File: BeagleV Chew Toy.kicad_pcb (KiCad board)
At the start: 2 copper layers, 69.2 x 59.8 mm, 151 parts, among them J1 Conn_02x05_Counter_Clockwise, J2 Conn_02x05_Counter_Clockwise, J3 Conn_02x05_Counter_Clockwise, U1 74HC245, U2 74HC245, U3 74HC245, U4 74HC245

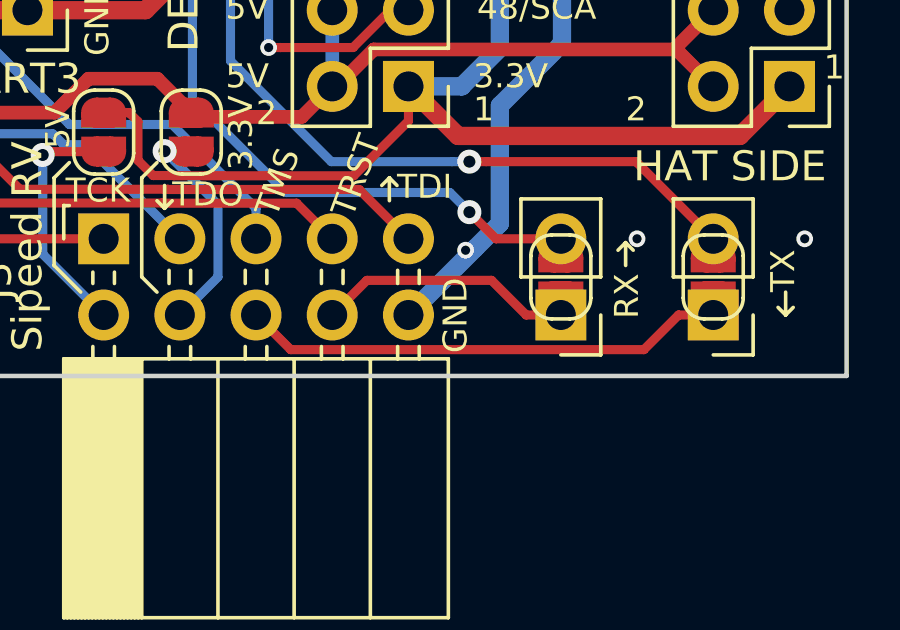
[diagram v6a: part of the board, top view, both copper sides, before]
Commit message: fixup: swap RX/TX on Sipeed connector
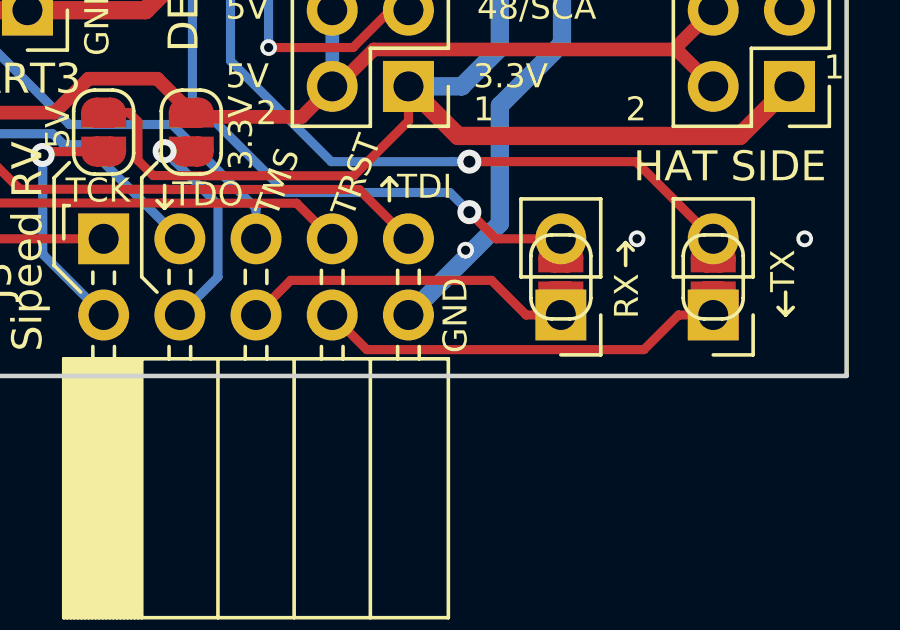
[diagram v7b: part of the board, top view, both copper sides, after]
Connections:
- JP36 pad 1: Net-(J3-Pad6) -> Net-(J3-Pad8)
- JP37 pad 1: Net-(J3-Pad6) -> Net-(J3-Pad8)
- JP38 pad 1: Net-(J3-Pad8) -> Net-(J3-Pad6)
- JP39 pad 1: Net-(J3-Pad8) -> Net-(J3-Pad6)
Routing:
- net Net-(J3-Pad8): track 8.58 -> 13.7 mm
- net Net-(J3-Pad6): track 16.2 -> 11.1 mm
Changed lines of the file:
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@@
       ))
     (pad 1 smd custom (at -0.65 0 90) (size 1 0.5) (layers Top F.Mask)
-      (net 56 "Net-(J3-Pad8)") (zone_connect 2)
+      (net 57 "Net-(J3-Pad6)") (zone_connect 2)
       (options (clearance outline) (anchor rect))
       (primitives
@@
       (net 20 /GPIO13/RX))
     (pad 1 thru_hole rect (at 0 0 180) (size 1.7 1.7) (drill 1) (layers *.Cu *.Mask)
-      (net 56 "Net-(J3-Pad8)"))
+      (net 57 "Net-(J3-Pad6)"))
     (model ${KISYS3DMOD}/Connector_PinHeader_2.54mm.3dshapes/PinHeader_1x02_P2.54mm_Vertical.wrl
       (at (xyz 0 0 0))
@@
       ))
     (pad 1 smd custom (at -0.65 0 90) (size 1 0.5) (layers Top F.Mask)
-      (net 57 "Net-(J3-Pad6)") (zone_connect 2)
+      (net 56 "Net-(J3-Pad8)") (zone_connect 2)
       (options (clearance outline) (anchor rect))
       (primitives
@@
       (net 21 /GPIO14/TX))
     (pad 1 thru_hole rect (at 0 0 180) (size 1.7 1.7) (drill 1) (layers *.Cu *.Mask)
-      (net 57 "Net-(J3-Pad6)"))
+      (net 56 "Net-(J3-Pad8)"))
     (model ${KISYS3DMOD}/Connector_PinHeader_2.54mm.3dshapes/PinHeader_1x02_P2.54mm_Vertical.wrl
       (at (xyz 0 0 0))
@@
   (segment (start 159.639 117.729) (end 159.639 97.663) (width 0.3048) (layer Top) (net 55))
   (segment (start 159.639 97.663) (end 160.5915 96.7105) (width 0.3048) (layer Top) (net 55))
-  (segment (start 184.3922 136.652) (end 185.547 136.652) (width 0.3048) (layer Top) (net 56))
-  (segment (start 183.237399 135.497199) (end 184.3922 136.652) (width 0.3048) (layer Top) (net 56))
-  (segment (start 179.081801 135.497199) (end 183.237399 135.497199) (width 0.3048) (layer Top) (net 56))
-  (segment (start 177.927 136.652) (end 179.081801 135.497199) (width 0.3048) (layer Top) (net 56))
-  (segment (start 189.4722 136.652) (end 190.627 136.652) (width 0.3048) (layer Top) (net 57))
-  (segment (start 188.317399 137.806801) (end 189.4722 136.652) (width 0.3048) (layer Top) (net 57))
-  (segment (start 176.541801 137.806801) (end 188.317399 137.806801) (width 0.3048) (layer Top) (net 57))
-  (segment (start 175.387 136.652) (end 176.541801 137.806801) (width 0.3048) (layer Top) (net 57))
+  (segment (start 189.4722 136.652) (end 190.627 136.652) (width 0.3048) (layer Top) (net 56))
+  (segment (start 188.317399 137.806801) (end 189.4722 136.652) (width 0.3048) (layer Top) (net 56))
+  (segment (start 177.927 136.652) (end 179.081801 137.806801) (width 0.3048) (layer Top) (net 56))
+  (segment (start 179.081801 137.806801) (end 188.317399 137.806801) (width 0.3048) (layer Top) (net 56))
+  (segment (start 175.387 136.652) (end 176.541801 135.497199) (width 0.3048) (layer Top) (net 57))
+  (segment (start 184.3922 136.652) (end 185.547 136.652) (width 0.3048) (layer Top) (net 57))
+  (segment (start 183.237399 135.497199) (end 184.3922 136.652) (width 0.3048) (layer Top) (net 57))
+  (segment (start 176.541801 135.497199) (end 183.237399 135.497199) (width 0.3048) (layer Top) (net 57))
   (via (at 172.339 131.191) (size 0.8) (drill 0.4) (layers Top Bottom) (net 58))
   (segment (start 173.213 131.191) (end 173.228 131.206) (width 0.3048) (layer Top) (net 58))

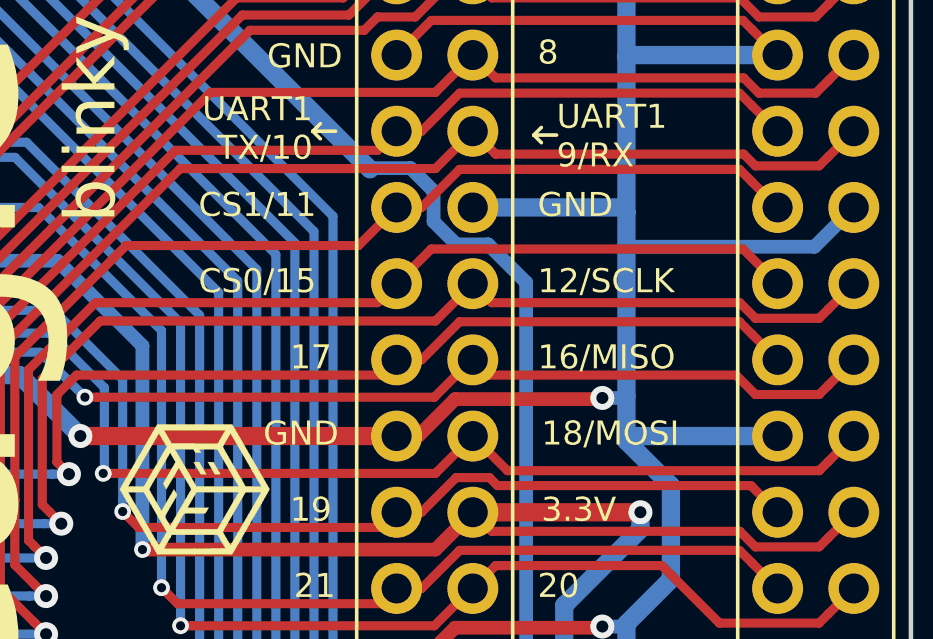
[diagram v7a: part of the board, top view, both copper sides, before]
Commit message: add questionmark to SPI pins in silk, generate gerbers
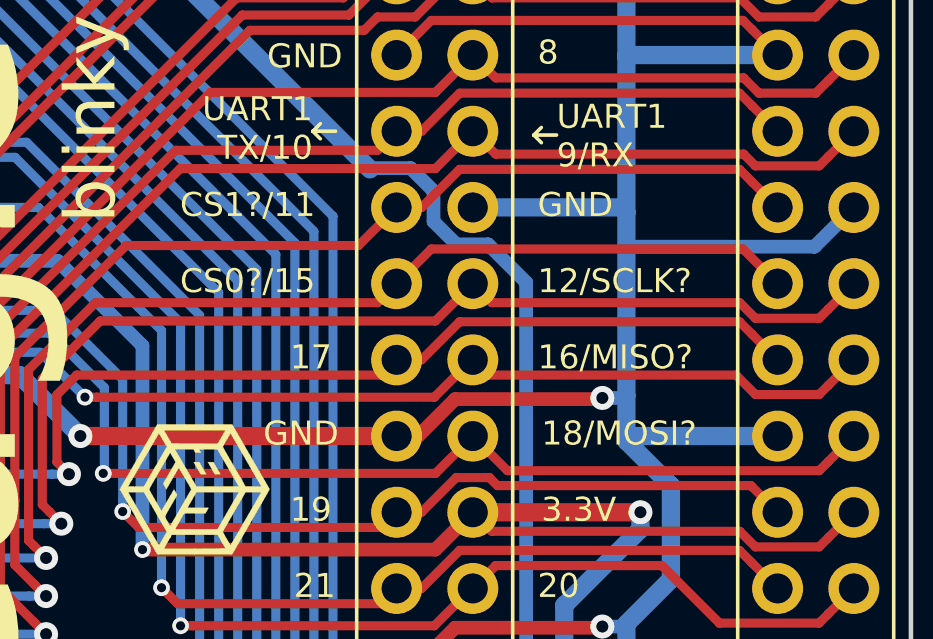
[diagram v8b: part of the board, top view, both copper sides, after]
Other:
- board text added: "12/SCLK?"
- board text added: "16/MISO?"
- board text added: "18/MOSI?"
- board text added: "CS0?/15"
- board text added: "CS1?/11"
- board text removed: "12/SCLK"
- board text removed: "16/MISO"
- board text removed: "18/MOSI"
- board text removed: "CS0/15"
- board text removed: "CS1/11"
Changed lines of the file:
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@@
     (effects (font (size 0.8 0.8) (thickness 0.1)) (justify left bottom))
   )
-  (gr_text 18/MOSI (at 182.753 106.553) (layer F.SilkS)
+  (gr_text 18/MOSI? (at 182.753 106.553) (layer F.SilkS)
     (effects (font (size 0.8 0.8) (thickness 0.1)) (justify left bottom))
   )
-  (gr_text 16/MISO (at 182.626 104.013) (layer F.SilkS)
+  (gr_text 16/MISO? (at 182.626 104.013) (layer F.SilkS)
     (effects (font (size 0.8 0.8) (thickness 0.1)) (justify left bottom))
   )
-  (gr_text 12/SCLK (at 182.626 101.473) (layer F.SilkS)
+  (gr_text 12/SCLK? (at 182.626 101.473) (layer F.SilkS)
     (effects (font (size 0.8 0.8) (thickness 0.1)) (justify left bottom))
   )
@@
     (effects (font (size 0.8 0.8) (thickness 0.1)) (justify left bottom))
   )
-  (gr_text CS0/15 (at 171.323 101.473) (layer F.SilkS)
+  (gr_text CS0?/15 (at 170.707 101.473) (layer F.SilkS)
     (effects (font (size 0.8 0.8) (thickness 0.1)) (justify left bottom))
   )
-  (gr_text CS1/11 (at 171.323 98.933) (layer F.SilkS)
+  (gr_text CS1?/11 (at 170.707 98.933) (layer F.SilkS)
     (effects (font (size 0.8 0.8) (thickness 0.1)) (justify left bottom))
   )
